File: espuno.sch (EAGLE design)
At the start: 62 parts, among them J1 ARDUINO_R3_SHIELD, T1 FDN340P, U1 ADS1115IDGST, U2 NCP1117ST50T3G, U3 LP2985-33DBVR, U4 FT232R, U5 LMV358IDGKR, U6 MCP73831, U7 TPS61200, X1 POWERSUPPLY_DC21MMX

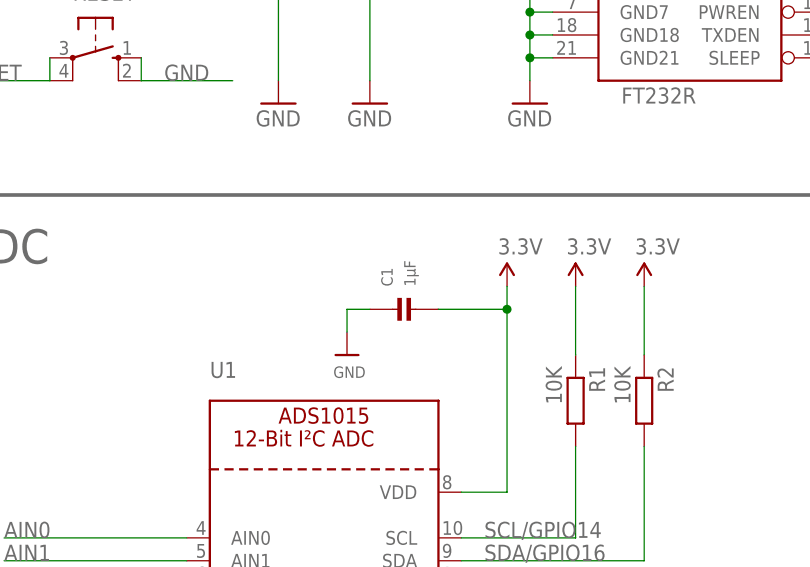
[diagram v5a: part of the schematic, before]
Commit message: Revise which size C1 is
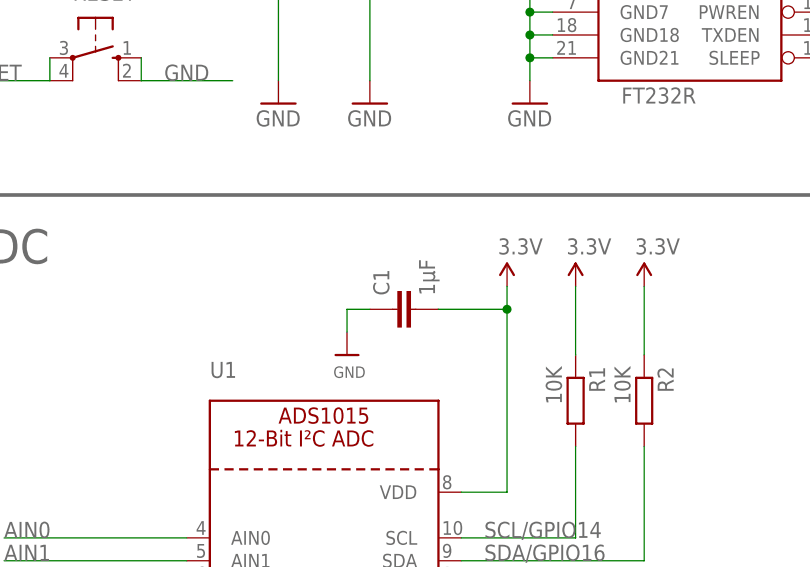
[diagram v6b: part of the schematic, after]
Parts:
- C1: device microbuilder:CAP_CERAMIC0805 -> SparkFun-Capacitors:CAP1206
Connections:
- net 3.3V: now also C1.2; no longer C1.P$2
- net GND: now also C1.1; no longer C1.P$1
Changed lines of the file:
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@@
 <part name="SUPPLY3" library="SparkFun-Aesthetics" deviceset="5V" device=""/>
 <part name="U1" library="microbuilder" deviceset="ADC_ADS1015" device="" value="ADS1115IDGST"/>
-<part name="C1" library="microbuilder" deviceset="CAP_CERAMIC" device="0805" value="1µF"/>
+<part name="C1" library="SparkFun-Capacitors" deviceset="CAP" device="1206" value="1µF"/>
 <part name="U$2" library="microbuilder" deviceset="GND" device=""/>
 <part name="R1" library="rcl" deviceset="R-EU_" device="M1206" value="10K"/>
@@
 <wire x1="60.96" y1="86.36" x2="66.04" y2="86.36" width="0.1524" layer="91"/>
 <wire x1="66.04" y1="86.36" x2="66.04" y2="106.68" width="0.1524" layer="91"/>
-<pinref part="C1" gate="G$1" pin="P$2"/>
+<pinref part="C1" gate="G$1" pin="2"/>
 <wire x1="66.04" y1="106.68" x2="58.42" y2="106.68" width="0.1524" layer="91"/>
 <wire x1="66.04" y1="106.68" x2="66.04" y2="109.22" width="0.1524" layer="91"/>
@@
 </segment>
 <segment>
-<pinref part="C1" gate="G$1" pin="P$1"/>
+<pinref part="C1" gate="G$1" pin="1"/>
 <pinref part="U$2" gate="G$1" pin="GND"/>
 <wire x1="50.8" y1="106.68" x2="48.26" y2="106.68" width="0.1524" layer="91"/>

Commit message: Change 100nf => 0.1uf
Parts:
- C1: value 1µF -> 0.1uf
- C2, C3: value 100n -> 0.1uf
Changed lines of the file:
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@@
 <part name="SUPPLY3" library="SparkFun-Aesthetics" deviceset="5V" device=""/>
 <part name="U1" library="microbuilder" deviceset="ADC_ADS1015" device="" value="ADS1115IDGST"/>
-<part name="C1" library="SparkFun-Capacitors" deviceset="CAP" device="1206" value="1µF"/>
+<part name="C1" library="SparkFun-Capacitors" deviceset="CAP" device="1206" value="0.1uf"/>
 <part name="U$2" library="microbuilder" deviceset="GND" device=""/>
 <part name="R1" library="rcl" deviceset="R-EU_" device="M1206" value="10K"/>
@@
 <part name="R3" library="rcl" deviceset="R-EU_" device="M1206" value="10K"/>
 <part name="U$6" library="microbuilder" deviceset="GND" device=""/>
-<part name="C2" library="rcl" deviceset="C-EU" device="C1206K" value="100n"/>
+<part name="C2" library="rcl" deviceset="C-EU" device="C1206K" value="0.1uf"/>
 <part name="GND7" library="supply1" deviceset="GND" device=""/>
 <part name="GND9" library="supply1" deviceset="GND" device=""/>
@@
 <part name="GND20" library="supply1" deviceset="GND" device=""/>
 <part name="GND18" library="supply1" deviceset="GND" device=""/>
-<part name="C3" library="rcl" deviceset="C-EU" device="C1206K" value="100n"/>
+<part name="C3" library="rcl" deviceset="C-EU" device="C1206K" value="0.1uf"/>
 <part name="GND21" library="supply1" deviceset="GND" device=""/>
 <part name="GND4" library="supply1" deviceset="GND" device=""/>

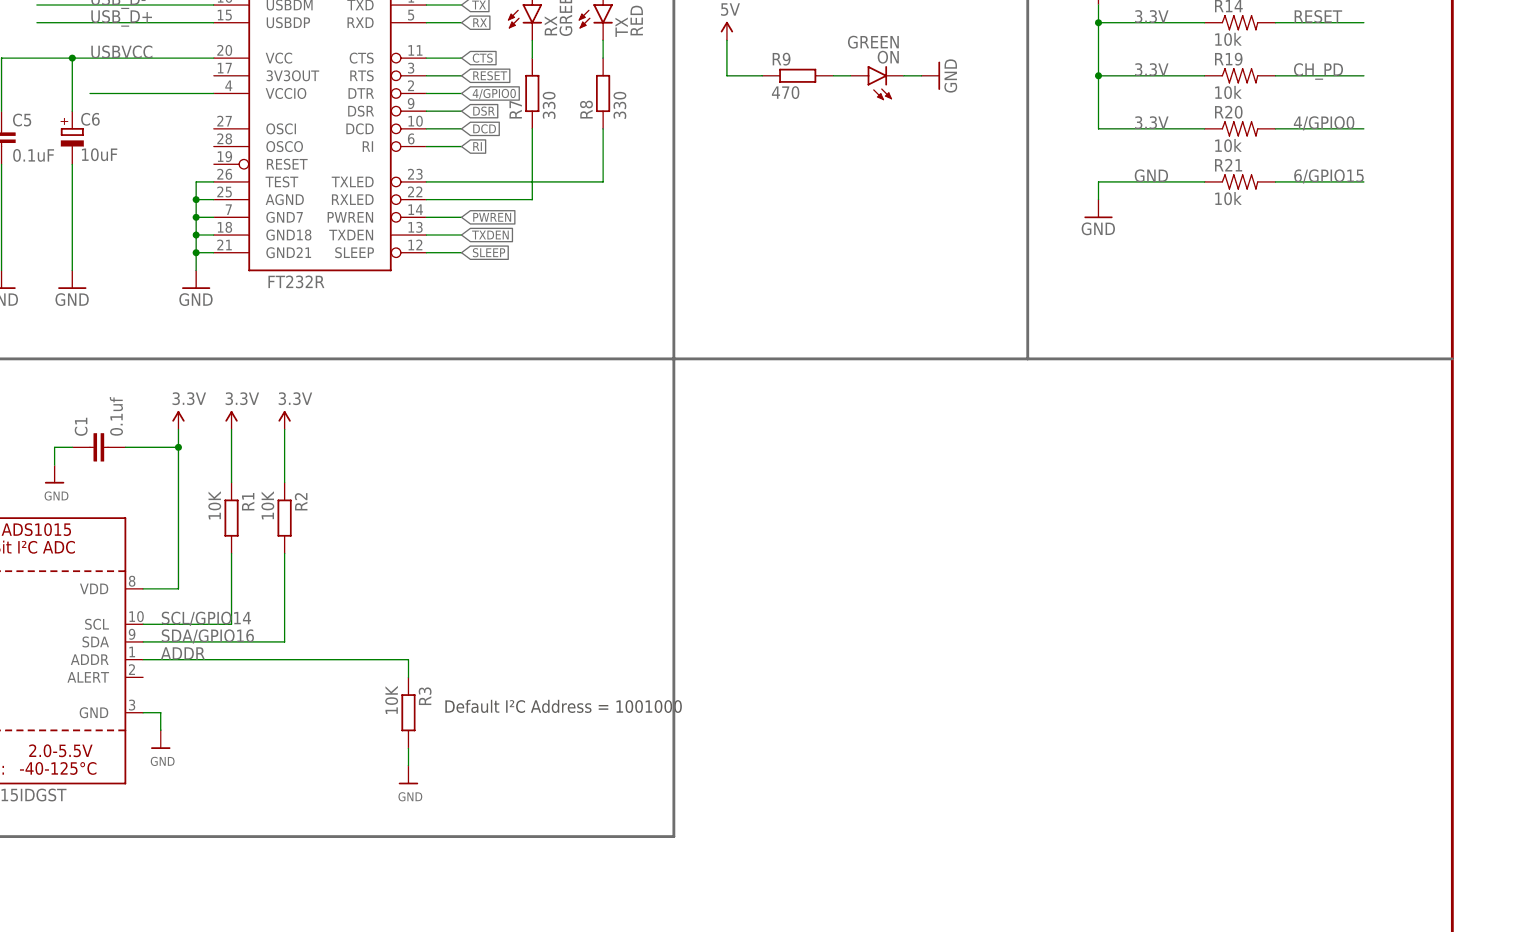
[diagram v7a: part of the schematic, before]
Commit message: Move i2c pullup resistors to Pullups section of schematic
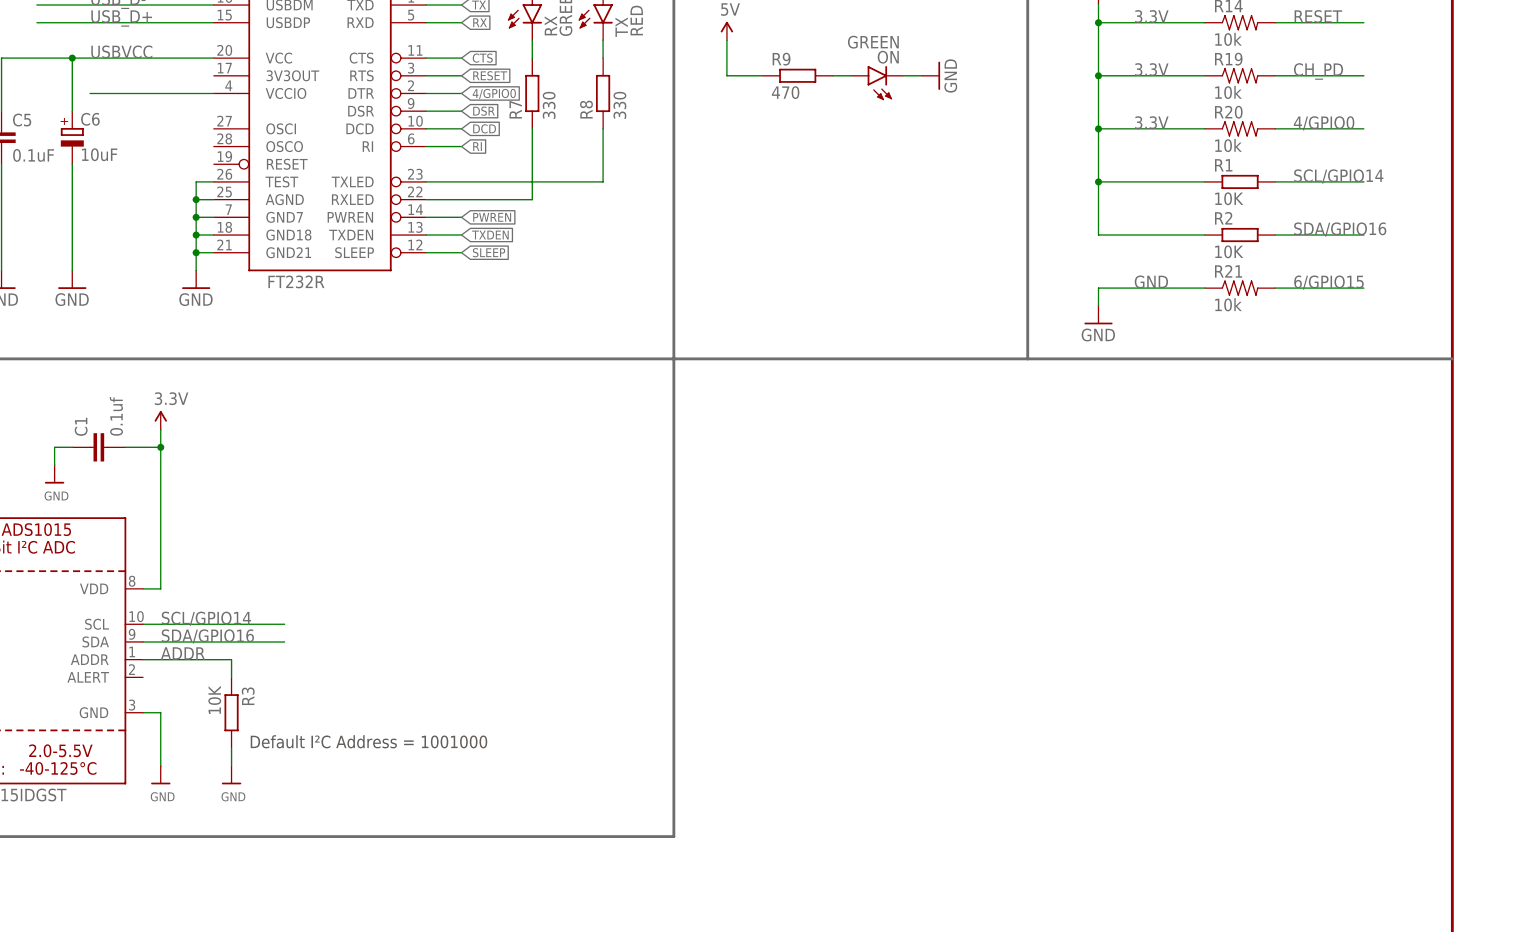
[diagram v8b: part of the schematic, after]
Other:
- moved on the sheet: R1, R2, R21, R3
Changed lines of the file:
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@@
 <part name="SUPPLY8" library="SparkFun-Aesthetics" deviceset="5V" device=""/>
 <part name="SUPPLY9" library="SparkFun-Aesthetics" deviceset="3.3V" device=""/>
-<part name="SUPPLY10" library="SparkFun-Aesthetics" deviceset="3.3V" device=""/>
-<part name="SUPPLY11" library="SparkFun-Aesthetics" deviceset="3.3V" device=""/>
 <part name="SUPPLY12" library="SparkFun-Aesthetics" deviceset="3.3V" device=""/>
 <part name="SUPPLY13" library="SparkFun-Aesthetics" deviceset="3.3V" device=""/>
@@
 <sheet>
 <plain>
-<text x="104.14" y="68.58" size="1.778" layer="97">Default I²C Address = 1001000</text>
+<text x="76.2" y="63.5" size="1.778" layer="97">Default I²C Address = 1001000</text>
 <text x="142.24" y="310.134" size="1.778" layer="97">UVLO 2.6V</text>
 <wire x1="0" y1="312.42" x2="86.36" y2="312.42" width="0.4064" layer="95"/>
@@
 <instance part="C1" gate="G$1" x="55.88" y="106.68" rot="R90"/>
 <instance part="U$2" gate="G$1" x="48.26" y="101.6"/>
-<instance part="R1" gate="G$1" x="73.66" y="96.52" rot="R270"/>
-<instance part="R2" gate="G$1" x="81.28" y="96.52" rot="R270"/>
-<instance part="U$5" gate="G$1" x="63.5" y="63.5"/>
-<instance part="R3" gate="G$1" x="99.06" y="68.58" rot="R270"/>
-<instance part="U$6" gate="G$1" x="99.06" y="58.42"/>
+<instance part="R1" gate="G$1" x="218.44" y="144.78"/>
+<instance part="R2" gate="G$1" x="218.44" y="137.16"/>
+<instance part="U$5" gate="G$1" x="63.5" y="58.42"/>
+<instance part="R3" gate="G$1" x="73.66" y="68.58" rot="R270"/>
+<instance part="U$6" gate="G$1" x="73.66" y="58.42"/>
 <instance part="C2" gate="G$1" x="172.72" y="266.7" smashed="yes" rot="R180">
 <attribute name="NAME" x="165.1" y="269.24" size="1.778" layer="95"/>
@@
 <instance part="SUPPLY7" gate="G$1" x="195.58" y="220.98"/>
 <instance part="SUPPLY8" gate="G$1" x="96.52" y="238.76"/>
-<instance part="SUPPLY9" gate="G$1" x="66.04" y="109.22"/>
-<instance part="SUPPLY10" gate="G$1" x="73.66" y="109.22"/>
-<instance part="SUPPLY11" gate="G$1" x="81.28" y="109.22"/>
+<instance part="SUPPLY9" gate="G$1" x="63.5" y="109.22"/>
 <instance part="SUPPLY12" gate="G$1" x="238.76" y="218.44"/>
 <instance part="SUPPLY13" gate="G$1" x="144.78" y="231.14"/>
@@
 <instance part="FRAME1" gate="G$1" x="0" y="193.04"/>
 <instance part="FRAME2" gate="G$1" x="0" y="0"/>
-<instance part="GND2" gate="1" x="198.12" y="139.7"/>
+<instance part="GND2" gate="1" x="198.12" y="124.46"/>
 <instance part="SUPPLY4" gate="G$1" x="198.12" y="170.18"/>
 <instance part="R14" gate="G$1" x="218.44" y="167.64"/>
 <instance part="R19" gate="G$1" x="218.44" y="160.02"/>
 <instance part="R20" gate="G$1" x="218.44" y="152.4"/>
-<instance part="R21" gate="G$1" x="218.44" y="144.78"/>
+<instance part="R21" gate="G$1" x="218.44" y="129.54"/>
 </instances>
 <busses>
@@
 <segment>
 <pinref part="U1" gate="G$1" pin="VDD"/>
-<wire x1="60.96" y1="86.36" x2="66.04" y2="86.36" width="0.1524" layer="91"/>
-<wire x1="66.04" y1="86.36" x2="66.04" y2="106.68" width="0.1524" layer="91"/>
+<wire x1="60.96" y1="86.36" x2="63.5" y2="86.36" width="0.1524" layer="91"/>
+<wire x1="63.5" y1="86.36" x2="63.5" y2="106.68" width="0.1524" layer="91"/>
 <pinref part="C1" gate="G$1" pin="2"/>
-<wire x1="66.04" y1="106.68" x2="58.42" y2="106.68" width="0.1524" layer="91"/>
-<wire x1="66.04" y1="106.68" x2="66.04" y2="109.22" width="0.1524" layer="91"/>
-<junction x="66.04" y="106.68"/>
+<wire x1="63.5" y1="106.68" x2="58.42" y2="106.68" width="0.1524" layer="91"/>
+<wire x1="63.5" y1="106.68" x2="63.5" y2="109.22" width="0.1524" layer="91"/>
+<junction x="63.5" y="106.68"/>
 <pinref part="SUPPLY9" gate="G$1" pin="3.3V"/>
-</segment>
-<segment>
-<pinref part="R2" gate="G$1" pin="1"/>
-<wire x1="81.28" y1="101.6" x2="81.28" y2="109.22" width="0.1524" layer="91"/>
-<pinref part="SUPPLY11" gate="G$1" pin="3.3V"/>
-</segment>
-<segment>
-<pinref part="R1" gate="G$1" pin="1"/>
-<wire x1="73.66" y1="101.6" x2="73.66" y2="109.22" width="0.1524" layer="91"/>
-<pinref part="SUPPLY10" gate="G$1" pin="3.3V"/>
 </segment>
 <segment>
@@
 <junction x="198.12" y="160.02"/>
 <junction x="198.12" y="167.64"/>
+<pinref part="R1" gate="G$1" pin="1"/>
+<wire x1="213.36" y1="144.78" x2="198.12" y2="144.78" width="0.1524" layer="91"/>
+<wire x1="198.12" y1="152.4" x2="198.12" y2="144.78" width="0.1524" layer="91"/>
+<pinref part="R2" gate="G$1" pin="1"/>
+<wire x1="213.36" y1="137.16" x2="198.12" y2="137.16" width="0.1524" layer="91"/>
+<wire x1="198.12" y1="144.78" x2="198.12" y2="137.16" width="0.1524" layer="91"/>
+<junction x="198.12" y="144.78"/>
+<junction x="198.12" y="152.4"/>
 </segment>
 </net>
@@
 <pinref part="U$5" gate="G$1" pin="GND"/>
 <wire x1="60.96" y1="68.58" x2="63.5" y2="68.58" width="0.1524" layer="91"/>
-<wire x1="63.5" y1="68.58" x2="63.5" y2="66.04" width="0.1524" layer="91"/>
+<wire x1="63.5" y1="68.58" x2="63.5" y2="60.96" width="0.1524" layer="91"/>
 </segment>
 <segment>
 <pinref part="R3" gate="G$1" pin="2"/>
 <pinref part="U$6" gate="G$1" pin="GND"/>
-<wire x1="99.06" y1="63.5" x2="99.06" y2="60.96" width="0.1524" layer="91"/>
+<wire x1="73.66" y1="63.5" x2="73.66" y2="60.96" width="0.1524" layer="91"/>
 </segment>
 <segment>
@@
 <segment>
 <pinref part="R21" gate="G$1" pin="1"/>
-<wire x1="213.36" y1="144.78" x2="198.12" y2="144.78" width="0.1524" layer="91"/>
-<label x="203.2" y="144.78" size="1.778" layer="95"/>
+<wire x1="213.36" y1="129.54" x2="198.12" y2="129.54" width="0.1524" layer="91"/>
+<label x="203.2" y="129.54" size="1.778" layer="95"/>
 <pinref part="GND2" gate="1" pin="GND"/>
-<wire x1="198.12" y1="144.78" x2="198.12" y2="142.24" width="0.1524" layer="91"/>
+<wire x1="198.12" y1="129.54" x2="198.12" y2="127" width="0.1524" layer="91"/>
 </segment>
 </net>
@@
 <segment>
 <pinref part="U1" gate="G$1" pin="SDA"/>
-<pinref part="R2" gate="G$1" pin="2"/>
 <wire x1="60.96" y1="78.74" x2="81.28" y2="78.74" width="0.1524" layer="91"/>
-<wire x1="81.28" y1="78.74" x2="81.28" y2="91.44" width="0.1524" layer="91"/>
 <label x="63.5" y="78.74" size="1.778" layer="95"/>
 </segment>
@@
 <label x="55.88" y="266.7" size="1.778" layer="95"/>
 </segment>
+<segment>
+<pinref part="R2" gate="G$1" pin="2"/>
+<wire x1="236.22" y1="137.16" x2="223.52" y2="137.16" width="0.1524" layer="91"/>
+<label x="226.06" y="137.16" size="1.778" layer="95"/>
+</segment>
 </net>
 <net name="SCL/GPIO14" class="0">
@@
 <segment>
 <pinref part="U1" gate="G$1" pin="SCL"/>
-<pinref part="R1" gate="G$1" pin="2"/>
-<wire x1="60.96" y1="81.28" x2="73.66" y2="81.28" width="0.1524" layer="91"/>
-<wire x1="73.66" y1="81.28" x2="73.66" y2="91.44" width="0.1524" layer="91"/>
+<wire x1="60.96" y1="81.28" x2="81.28" y2="81.28" width="0.1524" layer="91"/>
 <label x="63.5" y="81.28" size="1.778" layer="95"/>
 </segment>
@@
 <label x="55.88" y="264.16" size="1.778" layer="95"/>
 </segment>
+<segment>
+<pinref part="R1" gate="G$1" pin="2"/>
+<wire x1="236.22" y1="144.78" x2="223.52" y2="144.78" width="0.1524" layer="91"/>
+<label x="226.06" y="144.78" size="1.778" layer="95"/>
+</segment>
 </net>
 <net name="ADDR" class="0">
 <segment>
 <pinref part="U1" gate="G$1" pin="ADDR"/>
-<wire x1="60.96" y1="76.2" x2="99.06" y2="76.2" width="0.1524" layer="91"/>
+<wire x1="60.96" y1="76.2" x2="73.66" y2="76.2" width="0.1524" layer="91"/>
 <label x="63.5" y="76.2" size="1.778" layer="95"/>
 <pinref part="R3" gate="G$1" pin="1"/>
-<wire x1="99.06" y1="76.2" x2="99.06" y2="73.66" width="0.1524" layer="91"/>
+<wire x1="73.66" y1="76.2" x2="73.66" y2="73.66" width="0.1524" layer="91"/>
 </segment>
 </net>
@@
 <segment>
 <pinref part="R21" gate="G$1" pin="2"/>
-<wire x1="236.22" y1="144.78" x2="223.52" y2="144.78" width="0.1524" layer="91"/>
-<label x="226.06" y="144.78" size="1.778" layer="95"/>
-</segment>
-<segment>
+<wire x1="236.22" y1="129.54" x2="223.52" y2="129.54" width="0.1524" layer="91"/>
+<label x="226.06" y="129.54" size="1.778" layer="95"/>
+</segment>
+<segment>
